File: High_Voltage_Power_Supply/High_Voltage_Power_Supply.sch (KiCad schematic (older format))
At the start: 61 parts, among them J1 Conn_01x02_Female, J2 Conn_01x02_Female, J3 Conn_01x02_Female, J4 Conn_01x02_Female, J6 Conn_01x02_Female, Q1 Q_NMOS_GDS, U1 LT3751-TSSOP

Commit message: Finished the v2 of the schematic
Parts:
- removed J1, J4, J6, J? (x4): Conn_01x02_Female, Connector_PinHeader_2.54mm:PinHeader_1x02_P2.54mm_Vertical, symbol Connector:Conn_01x02_Female
- removed Q?: Q_NMOS_GDS, Package_TO_SOT_THT:TO-264-3_Vertical, symbol Device:Q_NMOS_GDS
- added J4: Conn_01x12_Female, Connector_PinHeader_2.54mm:PinHeader_1x12_P2.54mm_Vertical, symbol Connector:Conn_01x12_Female
- added Q3: Q_NIGBT_GCE, Package_TO_SOT_THT:TO-247-3_Vertical, symbol Device:Q_NIGBT_GCE
- added R11: 2.43k, Resistor_SMD:R_1206_3216Metric, symbol Device:R
- added U3, U4: MC14504B, Package_SO:SOIC-16_3.9x9.9mm_P1.27mm, symbol High_Voltage_Power_Supply:MC14504B
- added U5: ADCMP356, Package_TO_SOT_SMD:Analog_KS-4, symbol Comparator:ADCMP356
- added U6: ZXGD3004E6, Package_TO_SOT_SMD:SOT-23-6, symbol Driver_FET:ZXGD3004E6
- C2: renamed from C?; footprint Capacitor_SMD:C_1812_4532Metric -> Capacitor_THT:C_Rect_L31.5mm_W20.0mm_P27.50mm_MKS4; Link https://www.digikey.com/product-detail/en/murata-electronic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 -> https://www.digikey.com/en/products/detail/epcos-tdk-electr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; Voltage >1200V -> >600V
- R10: renamed from R17; value 4.87k -> 2.43k; Link https://www.digikey.com/product-detail/en/panasonic-electro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 -> https://www.digikey.com/en/products/detail/panasonic-electr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
- gave numbers to parts that had none: 24
- renumbered C4 to C11, C3 to C13, C2 to C15, C5 to C3, C6 to C4, J2 to J1, J3 to J2, R8 to R1, R3 to R13, R1 to R15, R11 to R17, R12 to R18, R7 to R2, R14 to R21, R13 to R23, R9 to R25, R10 to R26, R6 to R3, R5 to R4, R15 to R7, R16 to R8
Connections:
- net labels added: +5V, CHARGE, CHARGE_5V, CHARGE_IGN, CHARGE_IGN_5V, FIRE_5V, ~FAULT_5V~, ~FAULT_IGN_5V~
- wire segments 203 -> 252
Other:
- moved on the sheet: R10

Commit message: Updated BOM
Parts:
- C2: Link https://www.digikey.com/en/products/detail/epcos-tdk-electronics/B32774X1505K000/10468636 -> https://www.digikey.com/en/products/detail/epcos-tdk-electronics/B32774D1505K000/1884951
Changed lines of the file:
@@
 F 1 "5uF" H 8965 7205 50  0000 L CNN
 F 2 "Capacitor_THT:C_Rect_L31.5mm_W20.0mm_P27.50mm_MKS4" H 8888 7100 50  0001 C CNN
-F 3 "https://media.digikey.com/pdf/Data%20Sheets/TDK%20PDFs/B32774x,X,Y,Z_Series_DS.pdf" H 8850 7250 50  0001 C CNN
-F 4 "https://www.digikey.com/en/products/detail/epcos-tdk-electronics/B32774X1505K000/10468636" H 8850 7250 50  0001 C CNN "Link"
+F 3 "https://www.tdk-electronics.tdk.com/inf/20/20/db/fc_2009/MKP_B32774_778.pdf" H 8850 7250 50  0001 C CNN
+F 4 "https://www.digikey.com/en/products/detail/epcos-tdk-electronics/B32774D1505K000/1884951" H 8850 7250 50  0001 C CNN "Link"
 F 5 ">600V" H 8850 7250 50  0001 C CNN "Voltage"
 	1    8850 7250

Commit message: pcb fully layed out
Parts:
- added C17: 10nF, Capacitor_SMD:C_0603_1608Metric, symbol Device:C
- added C18: 10uF, Capacitor_SMD:C_1206_3216Metric, symbol Device:C
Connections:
- wire segments 252 -> 259
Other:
- moved on the sheet: Q3
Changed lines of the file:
@@
 L power:GND #PWR0131
 U 1 1 5F8F509E
-P 10500 8250
-F 0 "#PWR0131" H 10500 8000 50  0001 C CNN
-F 1 "GND" H 10505 8077 50  0000 C CNN
-F 2 "" H 10500 8250 50  0001 C CNN
-F 3 "" H 10500 8250 50  0001 C CNN
-	1    10500 8250
+P 10600 8700
+F 0 "#PWR0131" H 10600 8450 50  0001 C CNN
+F 1 "GND" H 10605 8527 50  0000 C CNN
+F 2 "" H 10600 8700 50  0001 C CNN
+F 3 "" H 10600 8700 50  0001 C CNN
+	1    10600 8700
 	1    0    0    -1
 $EndComp
 Wire Wire Line
 	10500 7750 10500 7950
-Wire Wire Line
-	10500 8250 10500 8050
 $Comp
 L Connector:Conn_01x02_Female J3
@@
 Wire Wire Line
 	9350 6950 9350 7750
-Wire Wire Line
-	9600 7750 9350 7750
 Connection ~ 9350 7750
 Wire Wire Line
 	9350 7750 9350 8600
-Wire Wire Line
-	10000 7750 10500 7750
 Wire Wire Line
 	9350 8900 9350 9550
@@
 Text GLabel 14700 5950 0    50   Input ~ 0
 Charged
-Wire Wire Line
-	9800 8700 9800 8050
 $Comp
 L Driver_FET:ZXGD3004E6 U6
@@
 	10400 8700 10400 8800
 Wire Wire Line
-	9800 8700 10200 8700
-Wire Wire Line
 	10200 8800 10200 8700
 Connection ~ 10200 8700
@@
 L Device:Q_NIGBT_GCE Q3
 U 1 1 5F9A2B3D
-P 9800 7850
-F 0 "Q3" V 10128 7850 50  0000 C CNN
-F 1 "Q_NIGBT_GCE" V 10037 7850 50  0000 C CNN
-F 2 "Package_TO_SOT_THT:TO-247-3_Vertical" H 10000 7950 50  0001 C CNN
-F 3 "https://www.littelfuse.com/~/media/electronics/datasheets/discrete_igbts/littelfuse_discrete_igbts_xpt_ixy_140n90c3_datasheet.pdf.pdf" H 9800 7850 50  0001 C CNN
-F 4 "https://www.digikey.com/en/products/detail/ixys/IXYX140N90C3/4321711" V 9800 7850 50  0001 C CNN "Link"
-F 5 ">600V" V 9800 7850 50  0001 C CNN "Voltage "
-	1    9800 7850
-	0    -1   -1   0
+P 10400 8350
+F 0 "Q3" V 10728 8350 50  0000 C CNN
+F 1 "Q_NIGBT_GCE" V 10637 8350 50  0000 C CNN
+F 2 "Package_TO_SOT_THT:TO-247-3_Vertical" H 10600 8450 50  0001 C CNN
+F 3 "https://www.littelfuse.com/~/media/electronics/datasheets/discrete_igbts/littelfuse_discrete_igbts_xpt_ixy_140n90c3_datasheet.pdf.pdf" H 10400 8350 50  0001 C CNN
+F 4 "https://www.digikey.com/en/products/detail/ixys/IXYX140N90C3/4321711" V 10400 8350 50  0001 C CNN "Link"
+F 5 ">600V" V 10400 8350 50  0001 C CNN "Voltage "
+	1    10400 8350
+	1    0    0    -1
 $EndComp
 $Comp
@@
 L power:+5V #PWR0139
 U 1 1 5FB9296F
-P 13950 6250
-F 0 "#PWR0139" H 13950 6100 50  0001 C CNN
-F 1 "+5V" H 13965 6423 50  0000 C CNN
-F 2 "" H 13950 6250 50  0001 C CNN
-F 3 "" H 13950 6250 50  0001 C CNN
-	1    13950 6250
+P 14150 6150
+F 0 "#PWR0139" H 14150 6000 50  0001 C CNN
+F 1 "+5V" H 14165 6323 50  0000 C CNN
+F 2 "" H 14150 6150 50  0001 C CNN
+F 3 "" H 14150 6150 50  0001 C CNN
+	1    14150 6150
 	1    0    0    -1
 $EndComp
@@
 	9250 4550 9250 4600
 Wire Wire Line
-	9250 4250 9750 4250
+	9250 4250 9500 4250
 $Comp
 L Device:R R11
@@
 	14650 6450 14650 6550
 Connection ~ 14650 6550
-Wire Wire Line
-	14700 6250 13950 6250
 $Comp
 L power:VCC #PWR0146
 U 1 1 600FC5B9
-P 14100 6150
-F 0 "#PWR0146" H 14100 6000 50  0001 C CNN
-F 1 "VCC" H 14117 6323 50  0000 C CNN
-F 2 "" H 14100 6150 50  0001 C CNN
-F 3 "" H 14100 6150 50  0001 C CNN
-	1    14100 6150
-	1    0    0    -1
-$EndComp
-Wire Wire Line
-	14700 6150 14700 6050
-Wire Wire Line
-	14700 6150 14100 6150
-Connection ~ 14700 6150
+P 13950 6250
+F 0 "#PWR0146" H 13950 6100 50  0001 C CNN
+F 1 "VCC" H 13967 6423 50  0000 C CNN
+F 2 "" H 13950 6250 50  0001 C CNN
+F 3 "" H 13950 6250 50  0001 C CNN
+	1    13950 6250
+	1    0    0    -1
+$EndComp
 Text GLabel 14150 5850 0    50   Input ~ 0
 ~FAULT_IGN_5V~
@@
 Wire Wire Line
 	14600 5750 14700 5750
-Text GLabel 14150 5650 0    50   Input ~ 0
-CHARGE_IGN
 Wire Wire Line
 	14700 5650 14150 5650
-Text GLabel 14550 5550 0    50   Input ~ 0
-CHARGE
 Wire Wire Line
 	14700 5550 14550 5550
-Text GLabel 14550 5450 0    50   Input ~ 0
-FIRE
 Wire Wire Line
 	14550 5450 14700 5450
@@
 F 3 "" H 6800 7400 50  0001 C CNN
 	1    6900 7400
-	1    0    0    -1
+	1    0    0    1
 $EndComp
 Wire Wire Line
 	5400 3550 5600 3550
+Wire Wire Line
+	9350 7750 10500 7750
+Wire Wire Line
+	10500 8150 10500 8050
+Wire Wire Line
+	10200 8350 10200 8700
+Wire Wire Line
+	10500 8550 10500 8600
+Wire Wire Line
+	10500 8600 10600 8600
+Wire Wire Line
+	10600 8600 10600 8700
+$Comp
+L Device:C C17
+U 1 1 5FF9BF8C
+P 9500 4400
+F 0 "C17" H 9615 4446 50  0000 L CNN
+F 1 "10nF" H 9615 4355 50  0000 L CNN
+F 2 "Capacitor_SMD:C_0603_1608Metric" H 9538 4250 50  0001 C CNN
+F 3 "https://www.murata.com/~/media/webrenewal/support/library/catalog/products/capacitor/mlcc/c02e.ashx?la=en-us" H 9500 4400 50  0001 C CNN
+F 4 "https://www.digikey.com/product-detail/en/murata-electronics/GRM1885C1H103JA01D/490-9666-1-ND/4934772" H 9500 4400 50  0001 C CNN "Link"
+	1    9500 4400
+	1    0    0    -1
+$EndComp
+Connection ~ 9500 4250
+Wire Wire Line
+	9500 4250 9750 4250
+$Comp
+L power:GND #PWR0147
+U 1 1 5FFA0BA9
+P 9500 4650
+F 0 "#PWR0147" H 9500 4400 50  0001 C CNN
+F 1 "GND" H 9505 4477 50  0000 C CNN
+F 2 "" H 9500 4650 50  0001 C CNN
+F 3 "" H 9500 4650 50  0001 C CNN
+	1    9500 4650
+	1    0    0    -1
+$EndComp
+Wire Wire Line
+	9500 4650 9500 4550
+Text GLabel 14150 5650 0    50   Input ~ 0
+CHARGE_IGN_5V
+Text GLabel 14550 5550 0    50   Input ~ 0
+CHARGE_5V
+Text GLabel 14550 5450 0    50   Input ~ 0
+FIRE_5V
+Wire Wire Line
+	14700 6150 14700 6250
+Wire Wire Line
+	14700 6250 13950 6250
+Connection ~ 14700 6250
+Wire Wire Line
+	14700 6050 14300 6050
+Wire Wire Line
+	14300 6050 14300 6150
+Wire Wire Line
+	14300 6150 14150 6150
+$Comp
+L Device:C C18
+U 1 1 60088DD7
+P 11200 4250
+F 0 "C18" H 11315 4296 50  0000 L CNN
+F 1 "10uF" H 11315 4205 50  0000 L CNN
+F 2 "Capacitor_SMD:C_1206_3216Metric" H 11238 4100 50  0001 C CNN
+F 3 "https://search.murata.co.jp/Ceramy/image/img/A01X/G101/ENG/GRT31CR61H106ME01-01.pdf" H 11200 4250 50  0001 C CNN
+F 4 "https://www.digikey.com/product-detail/en/murata-electronics/GRT31CR61H106ME01L/490-12457-1-ND/5417158" H 11200 4250 50  0001 C CNN "Link"
+	1    11200 4250
+	1    0    0    -1
+$EndComp
+$Comp
+L power:+5V #PWR?
+U 1 1 60091D0B
+P 11200 4050
+F 0 "#PWR?" H 11200 3900 50  0001 C CNN
+F 1 "+5V" H 11215 4223 50  0000 C CNN
+F 2 "" H 11200 4050 50  0001 C CNN
+F 3 "" H 11200 4050 50  0001 C CNN
+	1    11200 4050
+	1    0    0    -1
+$EndComp
+$Comp
+L power:GND #PWR?
+U 1 1 6009217E
+P 11200 4450
+F 0 "#PWR?" H 11200 4200 50  0001 C CNN
+F 1 "GND" H 11205 4277 50  0000 C CNN
+F 2 "" H 11200 4450 50  0001 C CNN
+F 3 "" H 11200 4450 50  0001 C CNN
+	1    11200 4450
+	1    0    0    -1
+$EndComp
+Wire Wire Line
+	11200 4450 11200 4400
+Wire Wire Line
+	11200 4100 11200 4050
 $EndSCHEMATC

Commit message: Created V3 of the schematic
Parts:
- removed R10: 2.43k, Resistor_SMD:R_1206_3216Metric, symbol Device:R
- removed U5: ADCMP356, Package_TO_SOT_SMD:Analog_KS-4, symbol Comparator:ADCMP356
- added C1, C3, C5, C7: 1000uF, Capacitor_THT:CP_Radial_D18.0mm_P7.50mm, symbol Device:CP
- added C13: 10uF, Capacitor_SMD:C_1210_3225Metric, symbol Device:C
- added C14, C15: 150pF, Capacitor_SMD:C_1206_3216Metric, symbol Device:C
- added C16, C18: 0.1uF, Capacitor_SMD:C_1206_3216Metric, symbol Device:C
- added C22: 100uF, Capacitor_THT:CP_Radial_D8.0mm_P5.00mm, symbol Device:CP
- added C25, C26, C27, C28, C29, C30, C32, C33: 10uF, Capacitor_SMD:C_1206_3216Metric, symbol Device:C
- added C37: 10nF, Capacitor_SMD:C_0603_1608Metric, symbol Device:C
- added D3: B3100-13-F, Diode_SMD:D_SMC, symbol Device:D_Schottky
- added L1: 33uH, Inductor_SMD:L_Bourns_SRR1260, symbol Device:L
- added Q2: Q_NMOS_GDS, Package_TO_SOT_THT:TO-264-3_Vertical, symbol Device:Q_NMOS_GDS
- added R14: 36.5k, Resistor_SMD:R_0603_1608Metric, symbol Device:R
- added R25, R26, R27: 4.7k, Resistor_SMD:R_1206_3216Metric, symbol Device:R
- added R5: 100k, Resistor_SMD:R_0603_1608Metric, symbol Device:R
- added R9: 4.87k, Resistor_SMD:R_1206_3216Metric, symbol Device:R
- added U10: ADR3412, Package_TO_SOT_SMD:SOT-23-6, symbol High_Voltage_Power_Supply:ADR3412
- added U11: LMR16030S, Package_SO:SOIC-8-1EP_3.9x4.9mm_P1.27mm_EP2.41x3.3mm_ThermalVias, symbol High_Voltage_Power_Supply:LMR16030S
- added U3: ZXGD3004E6, Package_TO_SOT_SMD:SOT-23-6, symbol Driver_FET:ZXGD3004E6
- added U7, U8: LM7805, Package_TO_SOT_SMD:SOT-223-3_TabPin2, symbol Regulator_Linear:LM7805_TO220
- added U9: LMV331, Package_TO_SOT_SMD:SOT-353_SC-70-5, symbol Comparator:LMV331
- C17: value 10nF -> 0.1uF; footprint Capacitor_SMD:C_0603_1608Metric -> Capacitor_SMD:C_1206_3216Metric; Link https://www.digikey.com/product-detail/en/murata-electronic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 -> https://www.digikey.com/en/products/detail/murata-electroni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
- J4: Link (none) -> https://www.digikey.com/en/products/detail/adam-tech/PH1-12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
- R11: value 2.43k -> 4.87k; Link https://www.digikey.com/en/products/detail/panasonic-electr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 -> https://www.digikey.com/product-detail/en/panasonic-electro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
- renumbered C3 to C10, C6 to C11, C5 to C12, C2 to C19, C8 to C2, C13 to C20, C14 to C21, C11 to C23, C12 to C24, C18 to C31, C1 to C34, C15 to C35, C16 to C36, C7 to C4, C10 to C6, C9 to C8, C4 to C9, Q2 to Q3, Q3 to Q4, R25 to R1, R12 to R10, R13 to R12, R14 to R13, R21 to R15, R22 to R16, R23 to R17, R24 to R18, R17 to R19, R26 to R2, R18 to R20, R19 to R21, R20 to R22, R15 to R23, R16 to R24, R4 to R28, R3 to R29, R27 to R3, R2 to R30, R1 to R31, R6 to R32, R5 to R33, R28 to R4, R7 to R6, R8 to R7, R9 to R8, U6 to U4, U3 to U5, U4 to U6
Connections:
- net labels added: +5VA, +5VD, Drive_in, Drive_out
- wire segments 259 -> 368
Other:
- moved on the sheet: C10, C11, C12, C19, C2, C20, C21, C23, C24, C31, C34, C35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

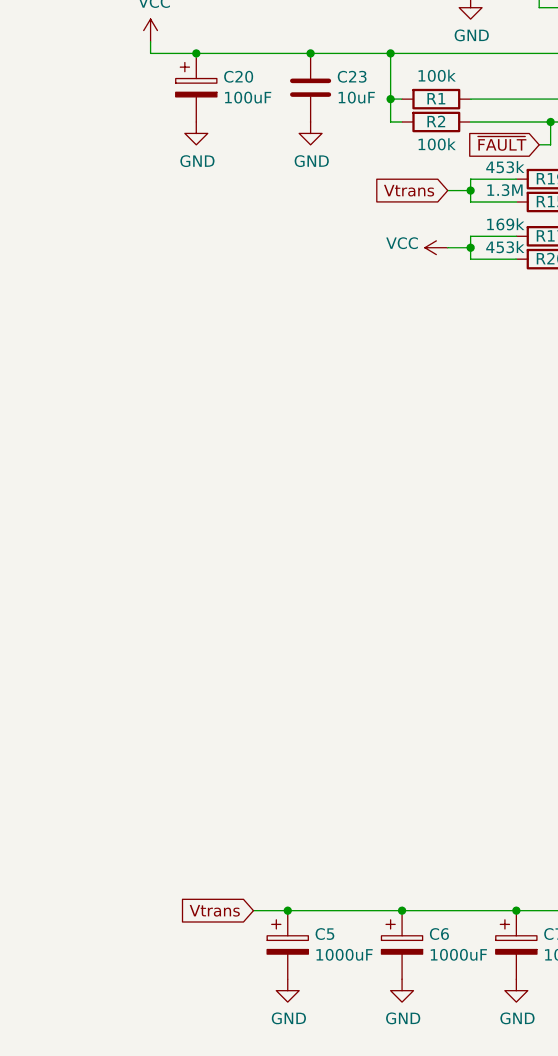
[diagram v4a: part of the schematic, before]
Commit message: schematic update with mounting holes
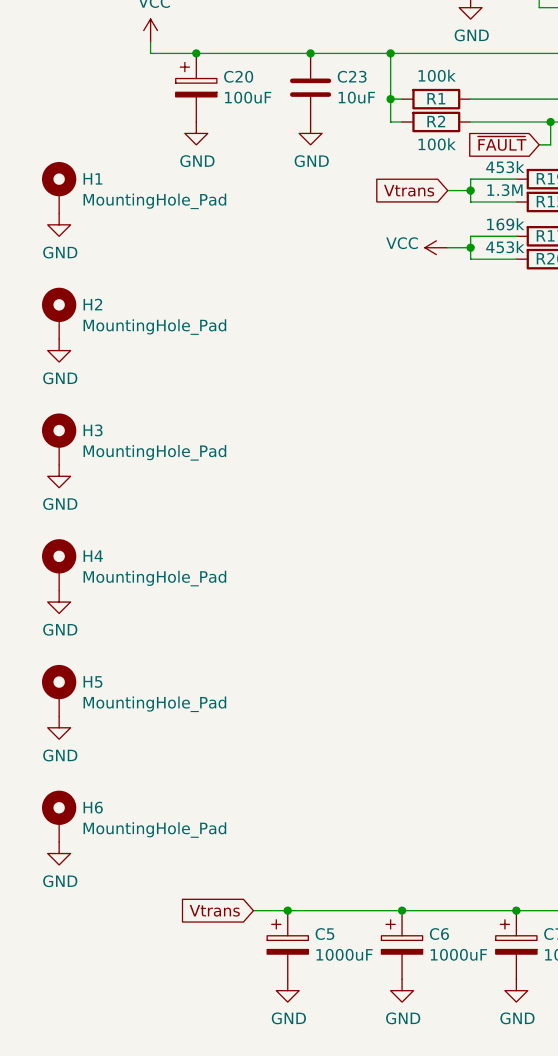
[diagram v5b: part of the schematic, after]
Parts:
- added H1, H2, H3, H4, H5, H6: MountingHole_Pad, MountingHole:MountingHole_3.2mm_M3_Pad_Via, symbol Mechanical:MountingHole_Pad
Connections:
- net GND: now also H1.1, H2.1, H3.1, H4.1, H5.1, H6.1
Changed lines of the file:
@@
 	0    1    1    0
 $EndComp
+$Comp
+L Mechanical:MountingHole_Pad H3
+U 1 1 60886234
+P 800 4450
+F 0 "H3" H 900 4499 50  0000 L CNN
+F 1 "MountingHole_Pad" H 900 4408 50  0000 L CNN
+F 2 "MountingHole:MountingHole_3.2mm_M3_Pad_Via" H 800 4450 50  0001 C CNN
+F 3 "~" H 800 4450 50  0001 C CNN
+	1    800  4450
+	1    0    0    -1
+$EndComp
+$Comp
+L power:GND #PWR0179
+U 1 1 608867CD
+P 800 4550
+F 0 "#PWR0179" H 800 4300 50  0001 C CNN
+F 1 "GND" H 805 4377 50  0000 C CNN
+F 2 "" H 800 4550 50  0001 C CNN
+F 3 "" H 800 4550 50  0001 C CNN
+	1    800  4550
+	1    0    0    -1
+$EndComp
+$Comp
+L Mechanical:MountingHole_Pad H4
+U 1 1 608D3F97
+P 800 5000
+F 0 "H4" H 900 5049 50  0000 L CNN
+F 1 "MountingHole_Pad" H 900 4958 50  0000 L CNN
+F 2 "MountingHole:MountingHole_3.2mm_M3_Pad_Via" H 800 5000 50  0001 C CNN
+F 3 "~" H 800 5000 50  0001 C CNN
+	1    800  5000
+	1    0    0    -1
+$EndComp
+$Comp
+L power:GND #PWR0180
+U 1 1 608D3F9D
+P 800 5100
+F 0 "#PWR0180" H 800 4850 50  0001 C CNN
+F 1 "GND" H 805 4927 50  0000 C CNN
+F 2 "" H 800 5100 50  0001 C CNN
+F 3 "" H 800 5100 50  0001 C CNN
+	1    800  5100
+	1    0    0    -1
+$EndComp
+$Comp
+L Mechanical:MountingHole_Pad H5
+U 1 1 608F41BF
+P 800 5550
+F 0 "H5" H 900 5599 50  0000 L CNN
+F 1 "MountingHole_Pad" H 900 5508 50  0000 L CNN
+F 2 "MountingHole:MountingHole_3.2mm_M3_Pad_Via" H 800 5550 50  0001 C CNN
+F 3 "~" H 800 5550 50  0001 C CNN
+	1    800  5550
+	1    0    0    -1
+$EndComp
+$Comp
+L power:GND #PWR0181
+U 1 1 608F41C5
+P 800 5650
+F 0 "#PWR0181" H 800 5400 50  0001 C CNN
+F 1 "GND" H 805 5477 50  0000 C CNN
+F 2 "" H 800 5650 50  0001 C CNN
+F 3 "" H 800 5650 50  0001 C CNN
+	1    800  5650
+	1    0    0    -1
+$EndComp
+$Comp
+L Mechanical:MountingHole_Pad H6
+U 1 1 60914351
+P 800 6100
+F 0 "H6" H 900 6149 50  0000 L CNN
+F 1 "MountingHole_Pad" H 900 6058 50  0000 L CNN
+F 2 "MountingHole:MountingHole_3.2mm_M3_Pad_Via" H 800 6100 50  0001 C CNN
+F 3 "~" H 800 6100 50  0001 C CNN
+	1    800  6100
+	1    0    0    -1
+$EndComp
+$Comp
+L power:GND #PWR0182
+U 1 1 60914357
+P 800 6200
+F 0 "#PWR0182" H 800 5950 50  0001 C CNN
+F 1 "GND" H 805 6027 50  0000 C CNN
+F 2 "" H 800 6200 50  0001 C CNN
+F 3 "" H 800 6200 50  0001 C CNN
+	1    800  6200
+	1    0    0    -1
+$EndComp
+$Comp
+L Mechanical:MountingHole_Pad H2
+U 1 1 6093532E
+P 800 3900
+F 0 "H2" H 900 3949 50  0000 L CNN
+F 1 "MountingHole_Pad" H 900 3858 50  0000 L CNN
+F 2 "MountingHole:MountingHole_3.2mm_M3_Pad_Via" H 800 3900 50  0001 C CNN
+F 3 "~" H 800 3900 50  0001 C CNN
+	1    800  3900
+	1    0    0    -1
+$EndComp
+$Comp
+L Mechanical:MountingHole_Pad H1
+U 1 1 60935F7D
+P 800 3350
+F 0 "H1" H 900 3399 50  0000 L CNN
+F 1 "MountingHole_Pad" H 900 3308 50  0000 L CNN
+F 2 "MountingHole:MountingHole_3.2mm_M3_Pad_Via" H 800 3350 50  0001 C CNN
+F 3 "~" H 800 3350 50  0001 C CNN
+	1    800  3350
+	1    0    0    -1
+$EndComp
+$Comp
+L power:GND #PWR0183
+U 1 1 6093E4BD
+P 800 4000
+F 0 "#PWR0183" H 800 3750 50  0001 C CNN
+F 1 "GND" H 805 3827 50  0000 C CNN
+F 2 "" H 800 4000 50  0001 C CNN
+F 3 "" H 800 4000 50  0001 C CNN
+	1    800  4000
+	1    0    0    -1
+$EndComp
+$Comp
+L power:GND #PWR0184
+U 1 1 609473E6
+P 800 3450
+F 0 "#PWR0184" H 800 3200 50  0001 C CNN
+F 1 "GND" H 805 3277 50  0000 C CNN
+F 2 "" H 800 3450 50  0001 C CNN
+F 3 "" H 800 3450 50  0001 C CNN
+	1    800  3450
+	1    0    0    -1
+$EndComp
 $EndSCHEMATC

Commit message: added new components and replaced out of stock ones in BOM
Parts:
- C10, C11, C12, C13, C9: Voltage (none) -> >100V
- C23, C24, C25, C26, C27, C28, C29, C30, C31, C32, C33: Link https://www.digikey.com/product-detail/en/murata-electronic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 -> https://www.digikey.com/en/products/detail/murata-electroni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; Voltage (none) -> >50V
- C34: Link https://www.digikey.com/product-detail/en/murata-electronic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 -> https://www.digikey.com/en/products/detail/tdk-corporation/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
- R17, R18: Link https://www.digikey.com/product-detail/en/panasonic-electro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 -> https://www.digikey.com/en/products/detail/susumu/RG2012P-1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
- R23, R24: Link https://www.digikey.com/product-detail/en/panasonic-electro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 -> https://www.digikey.com/en/products/detail/yageo/RT0603BRE0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
- R28, R29, R30, R31, R32, R33: Link https://www.digikey.com/product-detail/en/panasonic-electro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 -> https://www.digikey.com/en/products/detail/bourns-inc/CRE25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
- U7, U8: Link https://www.digikey.com/en/products/detail/texas-instruments/LM7805MPX-NOPB/6110827 -> https://www.digikey.com/en/products/detail/texas-instruments/LM7805MP-NOPB/6110582
- U9: Link (none) -> https://www.digikey.com/en/products/detail/stmicroelectroni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
